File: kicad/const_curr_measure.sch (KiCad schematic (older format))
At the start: 102 parts, among them IC1 XTR110AG, J1 Conn_02x02_Counter_Clockwise, J10 1-726386-2, J11 1-726386-2, J12 09061152911, J13 Conn_01x05, J2 1-726386-2, J3 Conn_01x12, J4 1-726386-2, J5 Conn_01x03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

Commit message: * addded Ibom * added normal bom
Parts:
- TP1: value DAC_SHDN -> 1018.68
- TP10: value DAC_OUT -> 1018.68
- TP11: value SENSE+VDIV -> 1018.68
- TP12: value VREF_O -> 1018.68
- TP13: value VREF_ADJ -> 1018.68
- TP14: value ARD_A0 -> 1018.68
- TP15: value GND -> 1018.68
- TP16: value 5V -> 1018.68
- TP17: value DAC_OUT_FULL_SWING -> 1018.68
- TP18: value 20_EN -> 1018.68
- TP19: value 100_EN -> 1018.68
- TP2: value EN_ADD_03 -> 1018.68
- TP20: value 1000_EN -> 1018.68
- TP21: value 10000_EN -> 1018.68
- TP22: value 20_EN_Rel -> 1018.68
- TP23: value 100_EN_Rel -> 1018.68
- TP24: value 1000_EN_Rel -> 1018.68
- TP25: value 10000_EN_Rel -> 1018.68
- TP26: value TMP_S_OW -> 1018.68
- TP27: value 20mA_SHN -> 1018.68
- TP28: value 100mA_SHN -> 1018.68
- TP29: value 1000mA_SHN -> 1018.68
- TP3: value SPI_CS -> 1018.68
- TP30: value 10000mA_SHN -> 1018.68
- TP31: value EN_ADD_01 -> 1018.68
- TP32: value EN_ADD_02 -> 1018.68
- TP33: value ROT_POT_A -> 1018.68
- TP34: value ROT_POT_B -> 1018.68
- TP35: value Range_Down -> 1018.68
- TP36: value Range_up -> 1018.68
- TP37: value Rot_Enc_Button -> 1018.68
- TP38: value 5V ref -> 1018.68
- TP4: value SPI_SCK -> 1018.68
- TP5: value SPI_MOSI -> 1018.68
- TP6: value SENSE-VDIV -> 1018.68
- TP7: value SPAN_ADJ -> 1018.68
- TP8: value SRC_RES -> 1018.68
- TP9: value ARD_A1 -> 1018.68
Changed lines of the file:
@@
 P 5200 1400
 F 0 "TP13" H 5352 1501 50  0000 L CNN
-F 1 "VREF_ADJ" H 5352 1410 50  0000 L CNN
+F 1 "1018.68" H 5352 1410 50  0000 L CNN
 F 2 "TestPoint:TestPoint_THTPad_D2.5mm_Drill1.2mm" H 5400 1400 50  0001 C CNN
 F 3 "~" H 5400 1400 50  0001 C CNN
@@
 P 5200 1000
 F 0 "TP12" H 5353 1101 50  0000 L CNN
-F 1 "VREF_O" H 5353 1010 50  0000 L CNN
+F 1 "1018.68" H 5353 1010 50  0000 L CNN
 F 2 "TestPoint:TestPoint_THTPad_D2.5mm_Drill1.2mm" H 5400 1000 50  0001 C CNN
 F 3 "~" H 5400 1000 50  0001 C CNN
@@
 P 2750 1600
 F 0 "TP7" H 2707 1608 50  0000 R CNN
-F 1 "SPAN_ADJ" H 2707 1699 50  0000 R CNN
+F 1 "1018.68" H 2707 1699 50  0000 R CNN
 F 2 "TestPoint:TestPoint_THTPad_D2.5mm_Drill1.2mm" H 2950 1600 50  0001 C CNN
 F 3 "~" H 2950 1600 50  0001 C CNN
@@
 P 2800 700
 F 0 "TP8" H 2953 801 50  0000 L CNN
-F 1 "SRC_RES" H 2953 710 50  0000 L CNN
+F 1 "1018.68" H 2953 710 50  0000 L CNN
 F 2 "TestPoint:TestPoint_THTPad_D2.5mm_Drill1.2mm" H 3000 700 50  0001 C CNN
 F 3 "~" H 3000 700 50  0001 C CNN
@@
 P 3900 6100
 F 0 "TP10" H 4052 6201 50  0000 L CNN
-F 1 "DAC_OUT" H 4052 6110 50  0000 L CNN
+F 1 "1018.68" H 4052 6110 50  0000 L CNN
 F 2 "TestPoint:TestPoint_THTPad_D2.5mm_Drill1.2mm" H 4100 6100 50  0001 C CNN
 F 3 "~" H 4100 6100 50  0001 C CNN
@@
 P 5600 9100
 F 0 "TP14" H 5753 9201 50  0000 L CNN
-F 1 "ARD_A0" H 5753 9110 50  0000 L CNN
+F 1 "1018.68" H 5753 9110 50  0000 L CNN
 F 2 "TestPoint:TestPoint_THTPad_D2.5mm_Drill1.2mm" H 5800 9100 50  0001 C CNN
 F 3 "~" H 5800 9100 50  0001 C CNN
@@
 P 2650 9100
 F 0 "TP9" H 2803 9201 50  0000 L CNN
-F 1 "ARD_A1" H 2803 9110 50  0000 L CNN
+F 1 "1018.68" H 2803 9110 50  0000 L CNN
 F 2 "TestPoint:TestPoint_THTPad_D2.5mm_Drill1.2mm" H 2850 9100 50  0001 C CNN
 F 3 "~" H 2850 9100 50  0001 C CNN
@@
 P 4850 8700
 F 0 "TP11" H 5002 8801 50  0000 L CNN
-F 1 "SENSE+VDIV" H 5002 8710 50  0000 L CNN
+F 1 "1018.68" H 5002 8710 50  0000 L CNN
 F 2 "TestPoint:TestPoint_THTPad_D2.5mm_Drill1.2mm" H 5050 8700 50  0001 C CNN
 F 3 "~" H 5050 8700 50  0001 C CNN
@@
 P 1950 8700
 F 0 "TP6" H 2102 8801 50  0000 L CNN
-F 1 "SENSE-VDIV" H 2102 8710 50  0000 L CNN
+F 1 "1018.68" H 2102 8710 50  0000 L CNN
 F 2 "TestPoint:TestPoint_THTPad_D2.5mm_Drill1.2mm" H 2150 8700 50  0001 C CNN
 F 3 "~" H 2150 8700 50  0001 C CNN
@@
 P 11800 6150
 F 0 "TP22" H 11952 6251 50  0000 L CNN
-F 1 "20_EN_Rel" H 11952 6160 50  0000 L CNN
+F 1 "1018.68" H 11952 6160 50  0000 L CNN
 F 2 "TestPoint:TestPoint_THTPad_D2.5mm_Drill1.2mm" H 12000 6150 50  0001 C CNN
 F 3 "~" H 12000 6150 50  0001 C CNN
@@
 P 11850 6300
 F 0 "TP23" H 12002 6401 50  0000 L CNN
-F 1 "100_EN_Rel" H 12002 6310 50  0000 L CNN
+F 1 "1018.68" H 12002 6310 50  0000 L CNN
 F 2 "TestPoint:TestPoint_THTPad_D2.5mm_Drill1.2mm" H 12050 6300 50  0001 C CNN
 F 3 "~" H 12050 6300 50  0001 C CNN
@@
 P 11900 6450
 F 0 "TP24" H 12053 6551 50  0000 L CNN
-F 1 "1000_EN_Rel" H 12053 6460 50  0000 L CNN
+F 1 "1018.68" H 12053 6460 50  0000 L CNN
 F 2 "TestPoint:TestPoint_THTPad_D2.5mm_Drill1.2mm" H 12100 6450 50  0001 C CNN
 F 3 "~" H 12100 6450 50  0001 C CNN
@@
 P 11950 6600
 F 0 "TP25" H 12103 6701 50  0000 L CNN
-F 1 "10000_EN_Rel" H 12103 6610 50  0000 L CNN
+F 1 "1018.68" H 12103 6610 50  0000 L CNN
 F 2 "TestPoint:TestPoint_THTPad_D2.5mm_Drill1.2mm" H 12150 6600 50  0001 C CNN
 F 3 "~" H 12150 6600 50  0001 C CNN
@@
 P 14550 2550
 F 0 "TP34" H 14703 2651 50  0000 L CNN
-F 1 "ROT_POT_B" H 14703 2560 50  0000 L CNN
+F 1 "1018.68" H 14703 2560 50  0000 L CNN
 F 2 "TestPoint:TestPoint_THTPad_D2.5mm_Drill1.2mm" H 14750 2550 50  0001 C CNN
 F 3 "~" H 14750 2550 50  0001 C CNN
@@
 P 14450 2700
 F 0 "TP33" H 14602 2801 50  0000 L CNN
-F 1 "ROT_POT_A" H 14602 2710 50  0000 L CNN
+F 1 "1018.68" H 14602 2710 50  0000 L CNN
 F 2 "TestPoint:TestPoint_THTPad_D2.5mm_Drill1.2mm" H 14650 2700 50  0001 C CNN
 F 3 "~" H 14650 2700 50  0001 C CNN
@@
 P 15250 5000
 F 0 "TP26" H 15403 5101 50  0000 L CNN
-F 1 "TMP_S_OW" H 15403 5010 50  0000 L CNN
+F 1 "1018.68" H 15403 5010 50  0000 L CNN
 F 2 "TestPoint:TestPoint_THTPad_D2.5mm_Drill1.2mm" H 15450 5000 50  0001 C CNN
 F 3 "~" H 15450 5000 50  0001 C CNN
@@
 P 13400 4500
 F 0 "TP15" H 13552 4601 50  0000 L CNN
-F 1 "GND" H 13552 4510 50  0000 L CNN
+F 1 "1018.68" H 13552 4510 50  0000 L CNN
 F 2 "TestPoint:TestPoint_THTPad_D2.5mm_Drill1.2mm" H 13600 4500 50  0001 C CNN
 F 3 "~" H 13600 4500 50  0001 C CNN
@@
 P 13400 4300
 F 0 "TP16" H 13553 4401 50  0000 L CNN
-F 1 "5V" H 13553 4310 50  0000 L CNN
+F 1 "1018.68" H 13553 4310 50  0000 L CNN
 F 2 "TestPoint:TestPoint_THTPad_D2.5mm_Drill1.2mm" H 13600 4300 50  0001 C CNN
 F 3 "~" H 13600 4300 50  0001 C CNN
@@
 P 2150 5850
 F 0 "TP4" H 2303 5951 50  0000 L CNN
-F 1 "SPI_SCK" H 2303 5860 50  0000 L CNN
+F 1 "1018.68" H 2303 5860 50  0000 L CNN
 F 2 "TestPoint:TestPoint_THTPad_D2.5mm_Drill1.2mm" H 2350 5850 50  0001 C CNN
 F 3 "~" H 2350 5850 50  0001 C CNN
@@
 P 2050 5700
 F 0 "TP3" H 2203 5801 50  0000 L CNN
-F 1 "SPI_CS" H 2203 5710 50  0000 L CNN
+F 1 "1018.68" H 2203 5710 50  0000 L CNN
 F 2 "TestPoint:TestPoint_THTPad_D2.5mm_Drill1.2mm" H 2250 5700 50  0001 C CNN
 F 3 "~" H 2250 5700 50  0001 C CNN
@@
 P 1850 5400
 F 0 "TP1" H 2003 5501 50  0000 L CNN
-F 1 "DAC_SHDN" H 2003 5410 50  0000 L CNN
+F 1 "1018.68" H 2003 5410 50  0000 L CNN
 F 2 "TestPoint:TestPoint_THTPad_D2.5mm_Drill1.2mm" H 2050 5400 50  0001 C CNN
 F 3 "~" H 2050 5400 50  0001 C CNN
@@
 P 2250 6000
 F 0 "TP5" H 2402 6101 50  0000 L CNN
-F 1 "SPI_MOSI" H 2402 6010 50  0000 L CNN
+F 1 "1018.68" H 2402 6010 50  0000 L CNN
 F 2 "TestPoint:TestPoint_THTPad_D2.5mm_Drill1.2mm" H 2450 6000 50  0001 C CNN
 F 3 "~" H 2450 6000 50  0001 C CNN
@@
 P 10350 6150
 F 0 "TP18" H 10503 6251 50  0000 L CNN
-F 1 "20_EN" H 10503 6160 50  0000 L CNN
+F 1 "1018.68" H 10503 6160 50  0000 L CNN
 F 2 "TestPoint:TestPoint_THTPad_D2.5mm_Drill1.2mm" H 10550 6150 50  0001 C CNN
 F 3 "~" H 10550 6150 50  0001 C CNN
@@
 P 10400 6300
 F 0 "TP19" H 10553 6401 50  0000 L CNN
-F 1 "100_EN" H 10553 6310 50  0000 L CNN
+F 1 "1018.68" H 10553 6310 50  0000 L CNN
 F 2 "TestPoint:TestPoint_THTPad_D2.5mm_Drill1.2mm" H 10600 6300 50  0001 C CNN
 F 3 "~" H 10600 6300 50  0001 C CNN
@@
 P 10450 6450
 F 0 "TP20" H 10602 6551 50  0000 L CNN
-F 1 "1000_EN" H 10602 6460 50  0000 L CNN
+F 1 "1018.68" H 10602 6460 50  0000 L CNN
 F 2 "TestPoint:TestPoint_THTPad_D2.5mm_Drill1.2mm" H 10650 6450 50  0001 C CNN
 F 3 "~" H 10650 6450 50  0001 C CNN
@@
 P 10500 6600
 F 0 "TP21" H 10652 6701 50  0000 L CNN
-F 1 "10000_EN" H 10652 6610 50  0000 L CNN
+F 1 "1018.68" H 10652 6610 50  0000 L CNN
 F 2 "TestPoint:TestPoint_THTPad_D2.5mm_Drill1.2mm" H 10700 6600 50  0001 C CNN
 F 3 "~" H 10700 6600 50  0001 C CNN
@@
 P 14400 6150
 F 0 "TP27" H 14553 6251 50  0000 L CNN
-F 1 "20mA_SHN" H 14553 6160 50  0000 L CNN
+F 1 "1018.68" H 14553 6160 50  0000 L CNN
 F 2 "TestPoint:TestPoint_THTPad_D2.5mm_Drill1.2mm" H 14600 6150 50  0001 C CNN
 F 3 "~" H 14600 6150 50  0001 C CNN
@@
 P 14450 6300
 F 0 "TP28" H 14603 6401 50  0000 L CNN
-F 1 "100mA_SHN" H 14603 6310 50  0000 L CNN
+F 1 "1018.68" H 14603 6310 50  0000 L CNN
 F 2 "TestPoint:TestPoint_THTPad_D2.5mm_Drill1.2mm" H 14650 6300 50  0001 C CNN
 F 3 "~" H 14650 6300 50  0001 C CNN
@@
 P 14500 6450
 F 0 "TP29" H 14652 6551 50  0000 L CNN
-F 1 "1000mA_SHN" H 14652 6460 50  0000 L CNN
+F 1 "1018.68" H 14652 6460 50  0000 L CNN
 F 2 "TestPoint:TestPoint_THTPad_D2.5mm_Drill1.2mm" H 14700 6450 50  0001 C CNN
 F 3 "~" H 14700 6450 50  0001 C CNN
@@
 P 14550 6600
 F 0 "TP30" H 14702 6701 50  0000 L CNN
-F 1 "10000mA_SHN" H 14702 6610 50  0000 L CNN
+F 1 "1018.68" H 14702 6610 50  0000 L CNN
 F 2 "TestPoint:TestPoint_THTPad_D2.5mm_Drill1.2mm" H 14750 6600 50  0001 C CNN
 F 3 "~" H 14750 6600 50  0001 C CNN
@@
 P 5700 5200
 F 0 "TP17" H 5852 5301 50  0000 L CNN
-F 1 "DAC_OUT_FULL_SWING" H 5852 5210 50  0000 L CNN
+F 1 "1018.68" H 5852 5210 50  0000 L CNN
 F 2 "TestPoint:TestPoint_THTPad_D2.5mm_Drill1.2mm" H 5900 5200 50  0001 C CNN
 F 3 "~" H 5900 5200 50  0001 C CNN
@@
 P 11800 7700
 F 0 "TP31" H 11953 7801 50  0000 L CNN
-F 1 "EN_ADD_01" H 11953 7710 50  0000 L CNN
+F 1 "1018.68" H 11953 7710 50  0000 L CNN
 F 2 "TestPoint:TestPoint_THTPad_D2.5mm_Drill1.2mm" H 12000 7700 50  0001 C CNN
 F 3 "~" H 12000 7700 50  0001 C CNN
@@
 P 11800 7800
 F 0 "TP32" H 11953 7901 50  0000 L CNN
-F 1 "EN_ADD_02" H 11953 7810 50  0000 L CNN
+F 1 "1018.68" H 11953 7810 50  0000 L CNN
 F 2 "TestPoint:TestPoint_THTPad_D2.5mm_Drill1.2mm" H 12000 7800 50  0001 C CNN
 F 3 "~" H 12000 7800 50  0001 C CNN
@@
 P 11800 7900
 F 0 "TP2" H 11953 8001 50  0000 L CNN
-F 1 "EN_ADD_03" H 11953 7910 50  0000 L CNN
+F 1 "1018.68" H 11953 7910 50  0000 L CNN
 F 2 "TestPoint:TestPoint_THTPad_D2.5mm_Drill1.2mm" H 12000 7900 50  0001 C CNN
 F 3 "~" H 12000 7900 50  0001 C CNN
@@
 P 14350 2850
 F 0 "TP36" H 14503 2951 50  0000 L CNN
-F 1 "Range_up" H 14503 2860 50  0000 L CNN
+F 1 "1018.68" H 14503 2860 50  0000 L CNN
 F 2 "TestPoint:TestPoint_THTPad_D2.5mm_Drill1.2mm" H 14550 2850 50  0001 C CNN
 F 3 "~" H 14550 2850 50  0001 C CNN
@@
 P 14250 3000
 F 0 "TP35" H 14402 3101 50  0000 L CNN
-F 1 "Range_Down" H 14402 3010 50  0000 L CNN
+F 1 "1018.68" H 14402 3010 50  0000 L CNN
 F 2 "TestPoint:TestPoint_THTPad_D2.5mm_Drill1.2mm" H 14450 3000 50  0001 C CNN
 F 3 "~" H 14450 3000 50  0001 C CNN
@@
 P 14650 2400
 F 0 "TP37" H 14803 2501 50  0000 L CNN
-F 1 "Rot_Enc_Button" H 14803 2410 50  0000 L CNN
+F 1 "1018.68" H 14803 2410 50  0000 L CNN
 F 2 "TestPoint:TestPoint_THTPad_D2.5mm_Drill1.2mm" H 14850 2400 50  0001 C CNN
 F 3 "~" H 14850 2400 50  0001 C CNN
@@
 P 3050 3700
 F 0 "TP38" H 3007 3708 50  0000 R CNN
-F 1 "5V ref" H 3007 3799 50  0000 R CNN
+F 1 "1018.68" H 3007 3799 50  0000 R CNN
 F 2 "TestPoint:TestPoint_THTPad_D2.5mm_Drill1.2mm" H 3250 3700 50  0001 C CNN
 F 3 "~" H 3250 3700 50  0001 C CNN

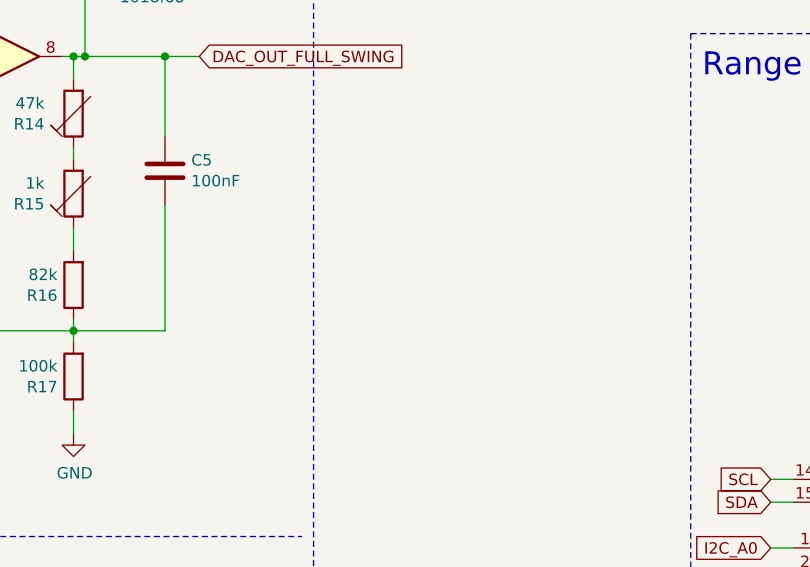
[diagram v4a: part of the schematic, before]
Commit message: * initial commit of "firmware"
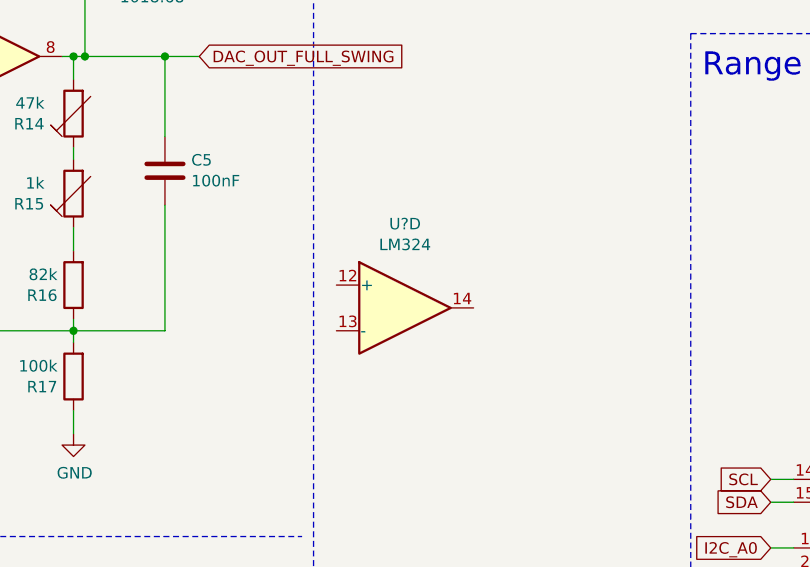
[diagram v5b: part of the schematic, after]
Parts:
- added U?: LM324, symbol Amplifier_Operational:LM324
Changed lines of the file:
@@
+	1    0    0    -1
+$EndComp
+$Comp
+L Amplifier_Operational:LM324 U?
+U 4 1 610CC904
+P 7100 6550
+F 0 "U?" H 7100 6917 50  0000 C CNN
+F 1 "LM324" H 7100 6826 50  0000 C CNN
+F 2 "" H 7050 6650 50  0001 C CNN
+F 3 "http://www.ti.com/lit/ds/symlink/lm2902-n.pdf" H 7150 6750 50  0001 C CNN
+	4    7100 6550
 	1    0    0    -1
 $EndComp

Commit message: current working changes for revision 0.2
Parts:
- removed C5: 100nF, Capacitor_THT:C_Rect_L7.2mm_W3.0mm_P5.00mm_FKS2_FKP2_MKS2_MKP2, symbol Device:C
- removed C9: 100nF, Capacitor_THT:C_Disc_D5.0mm_W2.5mm_P5.00mm, symbol Device:C
- removed D1, D2: D_Schottky, Diode_THT:D_A-405_P10.16mm_Horizontal, symbol Device:D_Schottky
- removed R1, R11, R17: 100k, Resistor_THT:R_Axial_DIN0207_L6.3mm_D2.5mm_P10.16mm_Horizontal, symbol Device:R
- removed R12, R2, R8: 10k, Resistor_THT:R_Axial_DIN0207_L6.3mm_D2.5mm_P10.16mm_Horizontal, symbol Device:R
- removed R13, R3, R4: 10k, Potentiometer_THT:Potentiometer_Piher_PT-6-V_Vertical, symbol Device:RTRIM
- removed R14: 47k, Potentiometer_THT:Potentiometer_Piher_PT-6-V_Vertical, symbol Device:RTRIM
- removed R15, R5: 1k, Potentiometer_THT:Potentiometer_Piher_PT-6-V_Vertical, symbol Device:RTRIM
- removed R16: 82k, Resistor_THT:R_Axial_DIN0207_L6.3mm_D2.5mm_P10.16mm_Horizontal, symbol Device:R
- removed RV1: 10k, Potentiometer_THT:Potentiometer_Piher_PT-6-V_Vertical, symbol Device:R_POT
- removed TP1, TP11, TP14, TP15, TP17, TP18, TP19, TP2, TP20, TP21, TP22, TP23, TP24, TP25, TP3, TP31, TP32, TP38, TP4, TP5, TP6, TP7, TP8, TP9: 1018.68, TestPoint:TestPoint_THTPad_D2.5mm_Drill1.2mm, symbol Connector:TestPoint_Probe
- removed U1: LM324, Package_DIP:DIP-14_W7.62mm_LongPads, symbol Amplifier_Operational:LM324
- removed U2: MCP4821, Package_DIP:DIP-8_W7.62mm_LongPads, symbol Analog_DAC:MCP4821
- removed U4: MCP3202, Package_DIP:DIP-8_W7.62mm_LongPads, symbol Analog_ADC:MCP3202
- removed U?: LM324, symbol Amplifier_Operational:LM324
- added 100nF: C, symbol Device:C
- added C?: 100nF, Capacitor_THT:C_Rect_L7.2mm_W3.0mm_P5.00mm_FKS2_FKP2_MKS2_MKP2, symbol Device:C
- added D? (x8): BAT54, Diode_THT:D_A-405_P10.16mm_Horizontal, symbol Device:D_Schottky
- added J? (x4): Conn_01x02, symbol Connector_Generic:Conn_01x02
- added J?: 09061316924, 09061316924, symbol SamacSys_Parts:09061316924
- added J?: Conn_01x04, symbol Connector_Generic:Conn_01x04
- added J?: Buf/Amp Bridged, symbol Connector_Generic:Conn_01x02
- added K? (x2): D3009, D3009, symbol SamacSys_Parts:D3009
- added R?: 100k, symbol Device:R_POT
- added R? (x2): 100k 0.1% 50ppm/K, Resistor_THT:R_Axial_DIN0207_L6.3mm_D2.5mm_P10.16mm_Horizontal, symbol Device:R
- added R? (x2): 900k 0.1% 50ppm/K, Resistor_THT:R_Axial_DIN0207_L6.3mm_D2.5mm_P10.16mm_Horizontal, symbol Device:R
- added R?: 24.9k 0.1% 50ppm/K, symbol Device:R
- added R? (x2): 10k, symbol Device:R
- added R? (x5): 4k7, symbol Device:R
- added R?: 100k, symbol Device:RTRIM
- added R?: 47k, symbol Device:R
- added R? (x2): 100k, symbol Device:R
- added RV? (x3): 20k, symbol Device:R_POT
- added U?: MCP4921, symbol Analog_DAC:MCP4921
- added U?: INA138, Package_TO_SOT_SMD:SOT-23-5, symbol Amplifier_Current:INA138
- added U? (x3): OP07, symbol Amplifier_Operational:OP07
- added U?: LT1011, symbol Comparator:LT1011
- added U? (x4): DG419xY, Package_SO:SOIC-8_3.9x4.9mm_P1.27mm, symbol Analog_Switch:DG419xY
- added U?: MCP3201, symbol Analog_ADC:MCP3201
- added U?: LD1117S33TR_SOT223, Package_TO_SOT_SMD:SOT-223-3_TabPin2, symbol Regulator_Linear:LD1117S33TR_SOT223
- D3, D4: value D_Schottky -> BAT54
- J1: value Conn_02x02_Counter_Clockwise -> Conn_2x2
- R18, R19: value R -> 4k7
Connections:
- net labels added: A_50V_ATT, BUF_OP_IN, B_50V_ATT, CURRENT_IN, DAC_LDAC, INPUT_SELECT, IN_SENSE_A, IN_SENSE_B, OVERRANGE_IND, SENSE_A_ATT, SENSE_B_ATT, VALUE_SELECT, VDD, VOLTAGE_IN
- net labels removed: +3.3V, 16m_Span, 4mA_Span, A0, A1, A2, A3, ADC0, ADC1, DAC_OUT, IOREF, OUT_SENSE_A, OUT_SENSE_B, Reset
- wire segments 419 -> 524
- no-connect marks 1 -> 0
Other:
- note added: "12 Bit DAC"
- note added: "ASW DG419"
- note added: "BUF OP OP07"
- note added: "Buffer Amplifier with Offset Adjustment\n"
- note added: "COMP LT1011"
- note added: "Channel Selection\n\n"
- note added: "DAC MCP4921"
- note added: "Error current should be about 1mA"
- note added: "High side shunt measurment"
- note added: "Maximium Input Voltage as designed: 50V\n"
- note added: "Optionl V=2 for use of 2.5V reference voltage"
- note added: "Overvoltage Detection"
- note added: "Position 1&2 for use with R9 & R10"
- note added: "Position 1&4, 2&3 for no span adjustment"
- note added: "Precision Low TK Resistors\n"
- note added: "R9 & R10 < 100R"
- note added: "REF02 Ref Voltage"
- note added: "Range Selection via Relay"
- note added: "TODO: DAC Vref+0.01V / VDD-0.04V Fix / If 5V REF DAC no OP amp needed"
- note added: "TODO: Span Adjust"
- note added: "To lower span \nfor span adjustment"
- note added: "offset off DAC can be compensated by span adjustment of XTR110AG"
- note removed: "ADC-Section"
- note removed: "DAC-Section"
- note removed: "Input Attentuation"
- note removed: "LCD Connector"
- note removed: "Maximium Input Voltage as designed: 10V\n"
- note removed: "Maximium Input Voltage as designed: 40V\n"
- note removed: "Range Switching"
- note removed: "Shield for Arduino that uses\nthe same pin disposition\nlike "Uno" board Rev 3."
- note removed: "V=1,22 for full 5V swing at 4,096V (max Swing of MCP4821)"
- moved on the sheet: A1, C1, C10, C2, C3, C4, C6, C7, C8, D3, D4, H1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
